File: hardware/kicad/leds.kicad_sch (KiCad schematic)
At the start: 10 parts

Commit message: Translate code, hardware and docs to English; bilingual dashboard
- tdm-logic i18n module: every dashboard text in English and Italian,
  chosen by `[display] language` in the profile (English by default, the
  TDM 850 profile keeps Italian); number formatting per language
- Slint fixed labels moved to a `Labels` global filled from the same table;
  `tdm-dash --language en|it`; reference screens regenerated in English with
  Italian check screens
- tdmctl, tdm-dash CLI, simulator scenarios, calibration errors and tools
  print English
- KiCad sheets, WireViz harnesses, perfboard plan and CAD comments in
  English, exports regenerated with the new names
- manual, research, ADRs and READMEs translated; files renamed (docs/manual,
  docs/research, English chapter and ADR names); status markers are now
  [VERIFIED] / [TO VERIFY] / [HYPOTHESIS]

Co-Authored-By: Claude Opus 5.5 <noreply@anthropic.com>
Claude-Session: https://claude.ai/code/session_01G9D4Wshjz9MkaThp4wsrGP
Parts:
- D801: value verde (freccia SX) -> green (left turn)
- D802: value verde (freccia DX) -> green (right turn)
- D803: value blu (abbaglianti) -> blue (high beam)
- D804: value verde (folle) -> green (neutral)
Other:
- note added: "Backup LEDs"
- note added: "Wired straight to the bike's 12 V lines: they light up even with the electronics off. The turn signals use one pair of wires like the original indicator (Ch–Dg): the flashing side feeds its LED, the other line goes to ground through the bulbs. The 1N4148 in series protects each LED from the reverse 12 V."
- note removed: "Collegati direttamente alle linee a 12 V della moto: si accendono anche a elettronica spenta. Le frecce usano una sola coppia di fili come la spia originale (Ch–Dg): la freccia accesa alimenta il suo LED, l'altra linea va a massa attraverso le lampadine. Il 1N4148 in serie protegge ogni LED dai 12 V inversi."
- note removed: "LED di backup"
- title: LED di backup -> Backup LEDs
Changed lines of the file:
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@@
 	(paper "A4")
 	(title_block
-		(title "LED di backup")
+		(title "Backup LEDs")
 		(date "2026-10-21")
 		(rev "0.1")
 		(company "tdm-dash · CERN-OHL-P-2.0")
-		(comment 1 "Foglio 8 di 8")
-		(comment 2 "Generato da hardware/kicad/generate.py: non modificare a mano")
+		(comment 1 "Sheet 8 of 8")
+		(comment 2 "Generated by hardware/kicad/generate.py: do not edit by hand")
 	)
 	(symbol
@@
 			)
 		)
-		(property "Value" "verde (freccia SX)"
+		(property "Value" "green (left turn)"
 			(at 88.9 58.674 0)
 			(effects
@@
 			)
 		)
-		(property "Value" "verde (freccia DX)"
+		(property "Value" "green (right turn)"
 			(at 88.9 84.074 0)
 			(effects
@@
 			)
 		)
-		(property "Value" "blu (abbaglianti)"
+		(property "Value" "blue (high beam)"
 			(at 177.8 58.674 0)
 			(effects
@@
 			)
 		)
-		(property "Value" "verde (folle)"
+		(property "Value" "green (neutral)"
 			(at 177.8 84.074 0)
 			(effects
@@
 		)
 	)
-	(text "LED di backup"
+	(text "Backup LEDs"
 		(exclude_from_sim no)
 		(at 10.16 12.7 0)
@@
 		)
 	)
-	(text "Collegati direttamente alle linee a 12 V della moto: si accendono anche a elettronica\nspenta. Le frecce usano una sola coppia di fili come la spia originale (Ch–Dg):\nla freccia accesa alimenta il suo LED, l'altra linea va a massa attraverso le lampadine.\nIl 1N4148 in serie protegge ogni LED dai 12 V inversi."
+	(text "Wired straight to the bike's 12 V lines: they light up even with the electronics\noff. The turn signals use one pair of wires like the original indicator (Ch–Dg):\nthe flashing side feeds its LED, the other line goes to ground through the bulbs.\nThe 1N4148 in series protects each LED from the reverse 12 V."
 		(exclude_from_sim no)
 		(at 10.16 17.78 0)

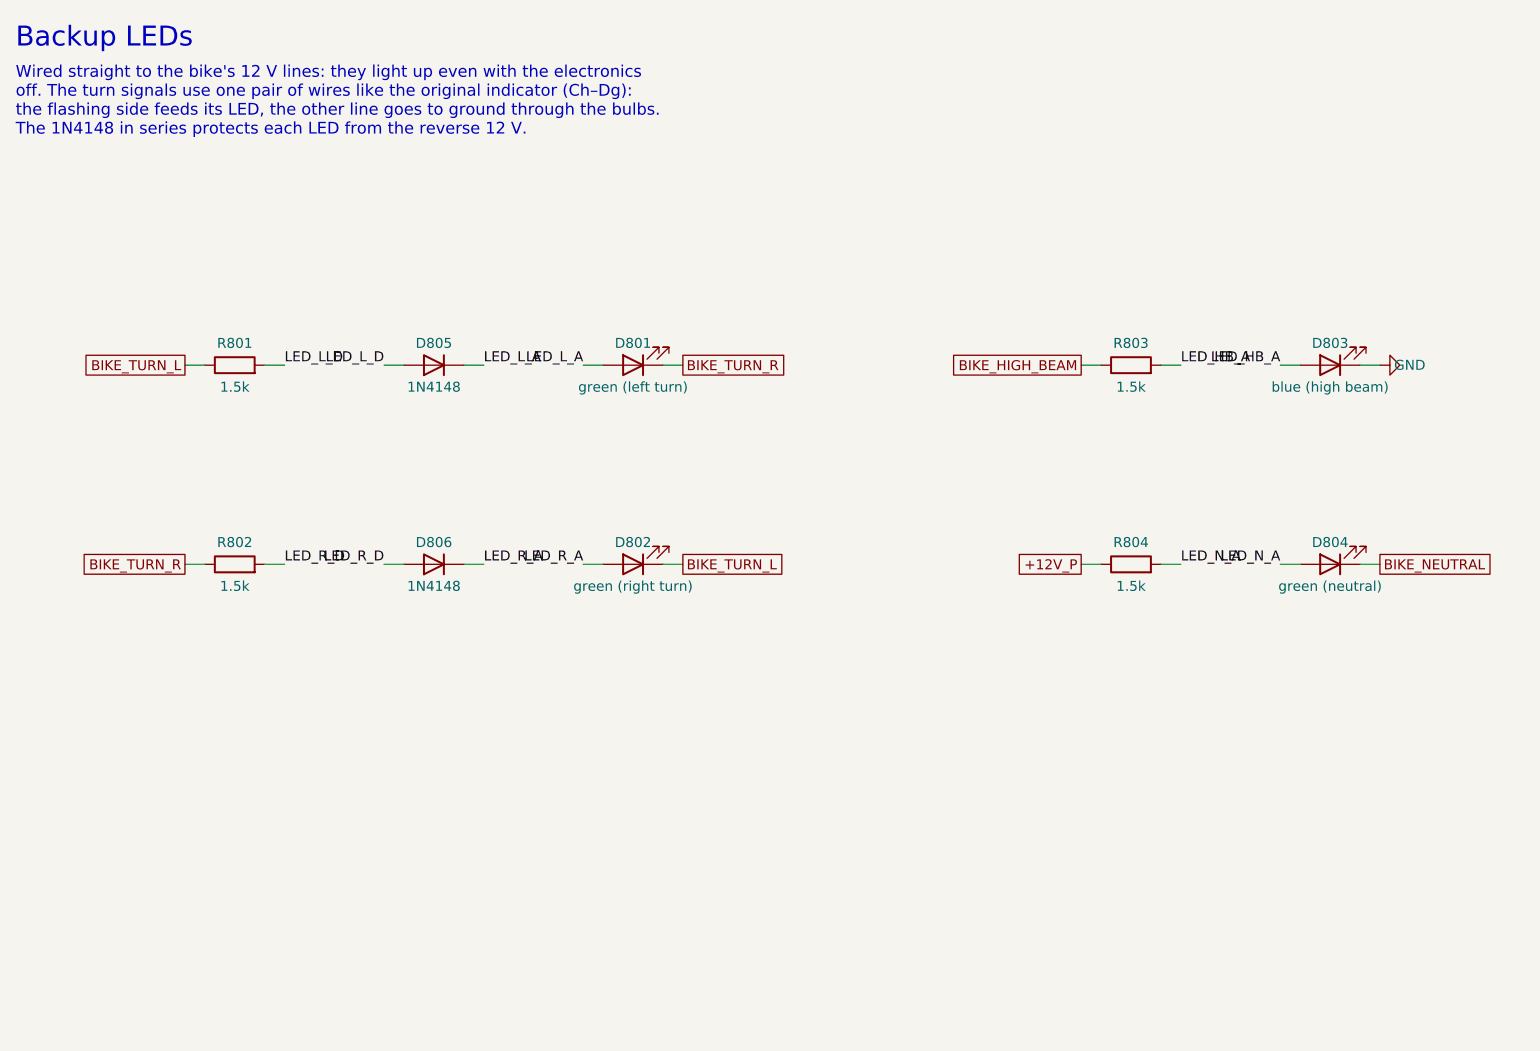
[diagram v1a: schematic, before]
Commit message: Schematic: drawn wires, block diagram, new title block
The sheets were a netlist in disguise: every pin ended in a short stub and
a label, so the circuits had to be pieced together by name, labels
overlapped, two sheets fell off the index page and the title block was
KiCad's default. The generator now draws the schematic:

- hardware/kicad/schgen: placement on the 50 mil grid, orthogonal wires,
  junctions, hierarchical ports, module and connector symbols with named
  pins; the drawing is normalised the way KiCad 9 reads it and checked
  against the declared netlist (no wire may connect anything else)
- hardware/kicad/sheets: one module per sheet, laid out left to right
  from the bike to the Pico; the root sheet is a block diagram whose
  wires are the signals between sheets
- tdm-dash.kicad_wks: frame and title block of the project
- symbols copied from KiCad 9.0.9 (vendor_symbols.py): the generator no
  longer needs KiCad installed
- export.sh: ERC, tools/check_netlist.py (KiCad's netlist is the declared
  one), check_pinmap.py, PDF and SVG on white, tools/check_svg_layout.py
  (no text over another text, a wire, the frame or the title block)

The circuit is unchanged: KiCad's netlist of the old and new schematic
has the same 56 nets (FRAM pins now follow the breakout header, R603/R604
pins swapped).

Co-Authored-By: Claude Opus 5.5 <noreply@anthropic.com>
Claude-Session: https://claude.ai/code/session_01G9D4Wshjz9MkaThp4wsrGP
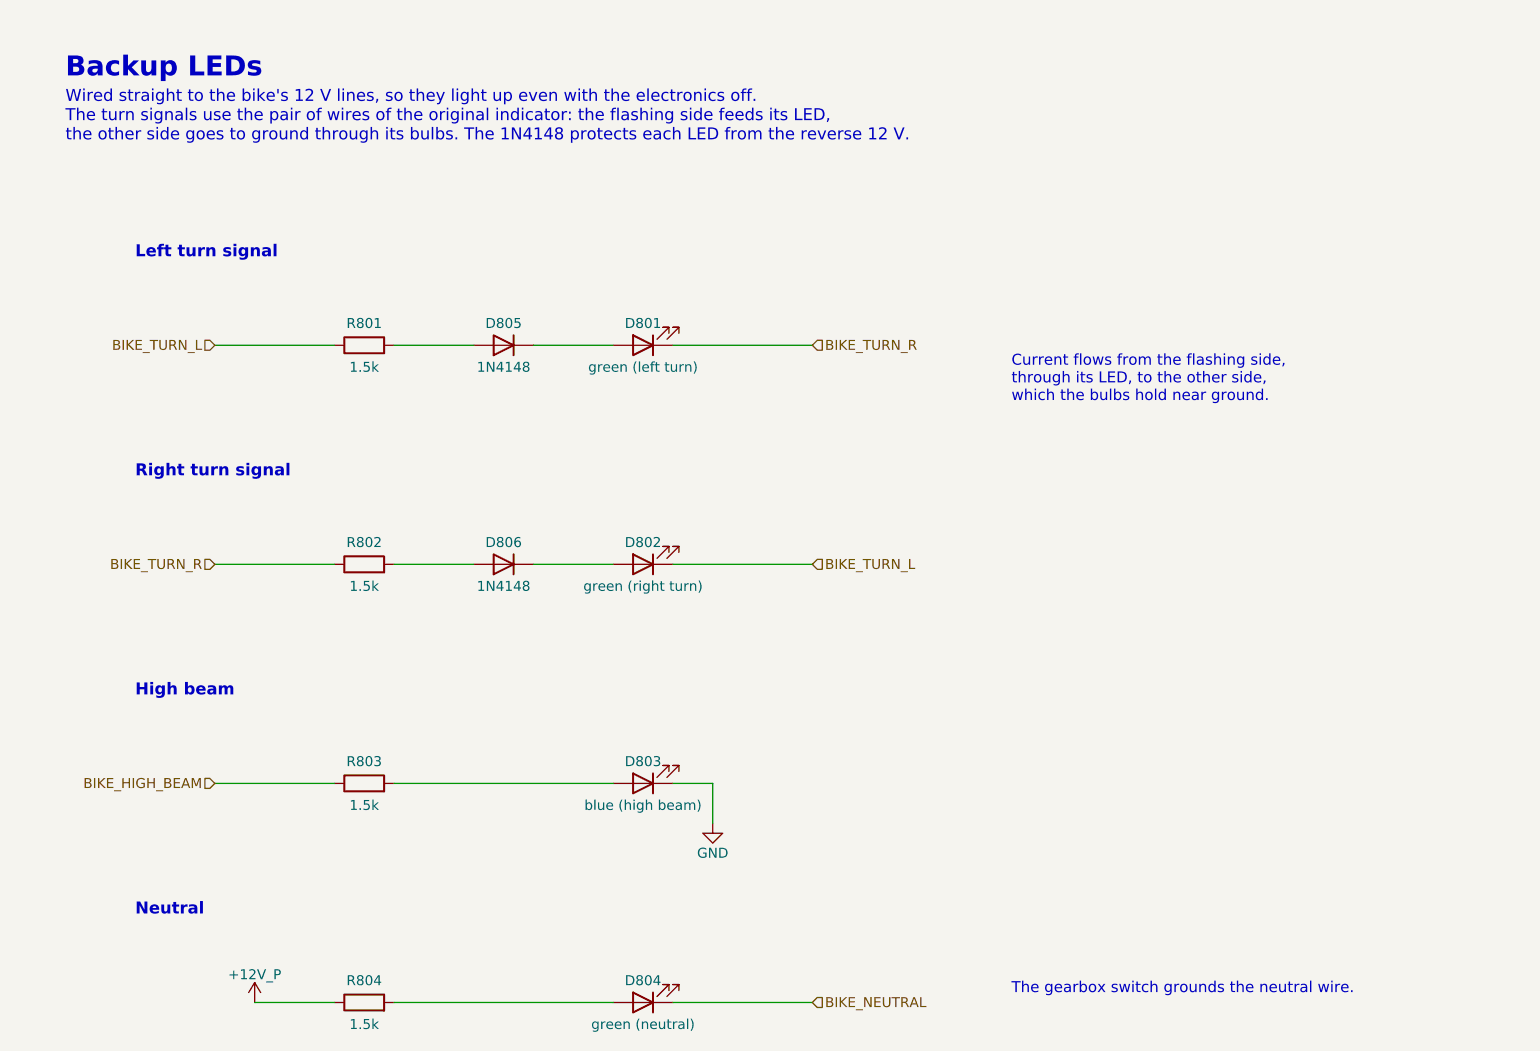
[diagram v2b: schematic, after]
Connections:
- net LED_HB_A: no longer names the net of D803.2 (A), R803.2
- net LED_L_A: no longer names the net of D801.2 (A), D805.1 (K)
- net LED_L_D: no longer names the net of D805.2 (A), R801.2
- net LED_N_A: no longer names the net of D804.2 (A), R804.2
- net LED_R_A: no longer names the net of D802.2 (A), D806.1 (K)
- net LED_R_D: no longer names the net of D806.2 (A), R802.2
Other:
- note added: "Current flows from the flashing side, through its LED, to the other side, which the bulbs hold near ground."
- note added: "High beam"
- note added: "Left turn signal"
- note added: "Neutral"
- note added: "Right turn signal"
- note added: "The gearbox switch grounds the neutral wire."
- note added: "Wired straight to the bike's 12 V lines, so they light up even with the electronics off. The turn signals use the pair of wires of the original indicator: the flashing side feeds its LED, the other side goes to ground through its bulbs. The 1N4148 protects each LED from the reverse 12 V."
- note removed: "Wired straight to the bike's 12 V lines: they light up even with the electronics off. The turn signals use one pair of wires like the original indicator (Ch–Dg): the flashing side feeds its LED, the other line goes to ground through the bulbs. The 1N4148 in series protects each LED from the reverse 12 V."
- company: tdm-dash · CERN-OHL-P-2.0 -> tdm-dash
